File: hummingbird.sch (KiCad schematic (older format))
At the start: 43 parts, among them J1 JST, J2 ANEMOMETER, J3 USB_B_Micro, J4 Expansion, J5 SWD_PROG, J6 microSD, J7 SOIC_CLIP, J8 Conn_01x01_Female, J9 Conn_Coaxial, SW1 SW_DPDT_x2, U1 MCP73831-2-OT, U2 AP2112K-3.3, U3 W25Q64JVSSIM, U4 ATSAMD21G18A-AUT, U5 RFM95W-915S2, U6 BMP388, Y1 32.768 Hz

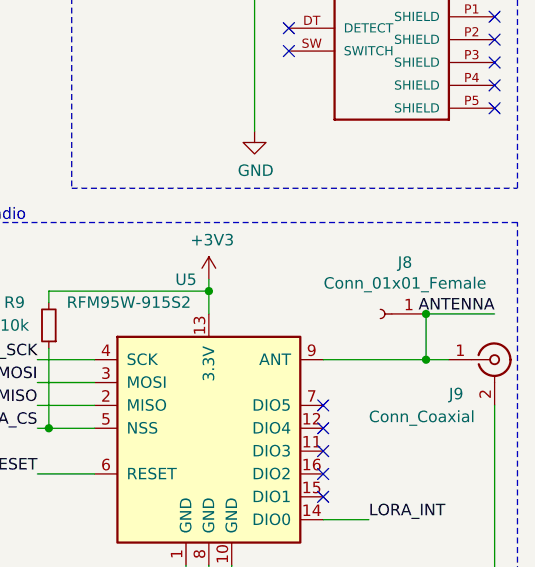
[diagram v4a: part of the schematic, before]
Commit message: add bmp388, SOICbyte and microSD footprint
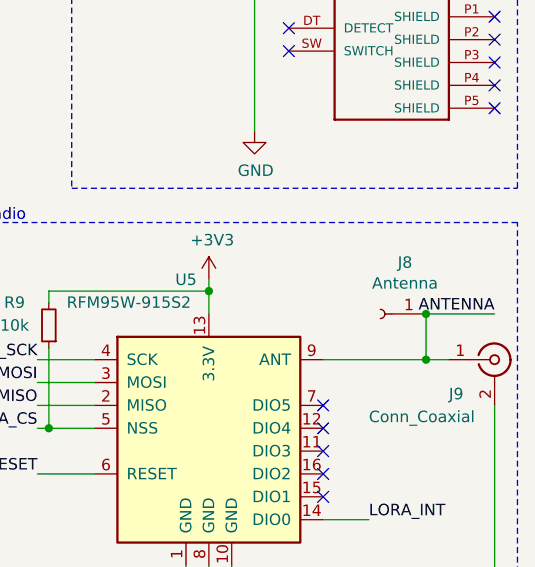
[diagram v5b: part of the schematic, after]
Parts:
- J6: footprint (none) -> microSD_503182-1852:MOLEX_503182-1852
- J7: footprint (none) -> footprints:SOIC_clipProgSmall
- J8: value Conn_01x01_Female -> Antenna; footprint (none) -> Connector_PinSocket_2.54mm:PinSocket_1x01_P2.54mm_Vertical
- U6: footprint (none) -> BMP388:PQFN50P200X200X80-10N
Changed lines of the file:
@@
 F 0 "U6" H 6800 6500 50  0000 C CNN
 F 1 "BMP388" H 6800 6400 50  0000 C CNN
-F 2 "" H 6800 5700 50  0001 L BNN
+F 2 "BMP388:PQFN50P200X200X80-10N" H 6800 5700 50  0001 L BNN
 F 3 "https://ae-bst.resource.bosch.com/media/_tech/media/datasheets/BST-BMP388-DS001.pdf" H 6800 5700 50  0001 L BNN
 F 4 "828-1079-1-ND" H 6800 5700 50  0001 L BNN "Field4"
@@
 F 0 "J6" H 9900 4467 50  0000 C CNN
 F 1 "microSD" H 9900 4376 50  0000 C CNN
-F 2 "" H 10400 3400 50  0001 L BNN
+F 2 "microSD_503182-1852:MOLEX_503182-1852" H 10400 3400 50  0001 L BNN
 F 3 "https://www.molex.com/pdm_docs/sd/5031821852_sd.pdf" H 10350 3750 50  0001 L BNN
 F 4 "MICRO SD NORMAL ULTRALOWPRO8CKTE" H 10350 4050 50  0001 L BNN "Field4"
@@
 P 9850 5150
 F 0 "J8" H 9742 4925 50  0000 C CNN
-F 1 "Conn_01x01_Female" H 9742 5016 50  0000 C CNN
-F 2 "" H 9850 5150 50  0001 C CNN
+F 1 "Antenna" H 9742 5016 50  0000 C CNN
+F 2 "Connector_PinSocket_2.54mm:PinSocket_1x01_P2.54mm_Vertical" H 9850 5150 50  0001 C CNN
 F 3 "~" H 9850 5150 50  0001 C CNN
 	1    9850 5150
@@
 F 0 "J7" H 4542 4375 50  0000 C CNN
 F 1 "SOIC_CLIP" H 4542 4466 50  0000 C CNN
-F 2 "" H 4650 4800 50  0001 C CNN
+F 2 "footprints:SOIC_clipProgSmall" H 4650 4800 50  0001 C CNN
 F 3 "https://hackaday.io/project/165917-soicbite-programmingdebug-connector-footprint" H 4650 4800 50  0001 C CNN
 	1    4650 4800

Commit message: copy all footprints to repo
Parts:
- C1, C10, C2, C3, C4, C5, C6, C7, C8, C9: footprint Capacitor_SMD:C_0603_1608Metric -> footprints:C_0603_1608Metric
- D1: footprint Diode_SMD:D_0603_1608Metric -> footprints:D_0603_1608Metric
- D2, D3, D4: footprint LED_SMD:LED_0603_1608Metric -> footprints:LED_0603_1608Metric
- J1: footprint (none) -> footprints:PinHeader_2x1mm_P2mm_SMD_RA
- J2: footprint Connector_PinHeader_2.54mm:PinHeader_1x03_P2.54mm_Vertical -> footprints:PinSocket_1x03_P2.54mm_Vertical
- J3: footprint (none) -> footprints:USB_Micro_B_Female_10118194-0001LF
- J4: footprint Connector_PinHeader_2.54mm:PinHeader_1x06_P2.54mm_Vertical -> footprints:PinSocket_1x06_P2.54mm_Vertical
- J5: footprint Connector_PinHeader_2.54mm:PinHeader_1x05_P2.54mm_Vertical -> footprints:PinSocket_1x05_P2.54mm_Vertical
- J8: footprint Connector_PinSocket_2.54mm:PinSocket_1x01_P2.54mm_Vertical -> footprints:PinSocket_1x01_P2.54mm_Vertical
- J9: footprint Connector_Coaxial:SMA_Molex_73251-1153_EdgeMount_Horizontal -> footprints:SMA_Molex_73251-1153_EdgeMount_Horizontal
- R1, R10, R2, R3, R4, R5, R6, R7, R8, R9: footprint Resistor_SMD:R_0603_1608Metric -> footprints:R_0603_1608Metric
- SW1: footprint (none) -> footprints:Switch_Slide_JS202011SCQN
- TP1, TP2: footprint TestPoint:TestPoint_Pad_D1.0mm -> footprints:TestPoint_Pad_D1.0mm
- U1, U2: footprint Package_TO_SOT_SMD:SOT-23-5 -> footprints:SOT-23-5
- U3: footprint Package_SO:SOIC-8_5.23x5.23mm_P1.27mm -> footprints:SOIC-8_5.23x5.23mm_P1.27mm
- U4: footprint Package_QFP:TQFP-48_7x7mm_P0.5mm -> footprints:TQFP-48_7x7mm_P0.5mm
- U5: footprint (none) -> footprints:RFM69HCW-XXXS2
- Y1: footprint Crystal:Crystal_SMD_3215-2Pin_3.2x1.5mm -> footprints:Crystal_SMD_3215-2Pin_3.2x1.5mm

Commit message: Add digikey part numbers
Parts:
- C1, C2, C3: DigiKey Part Number (none) -> 1276-1119-1-ND
- C10, C9: DigiKey Part Number (none) -> 1276-1182-1-ND
- C4, C5: DigiKey Part Number (none) -> 478-1167-1-ND
- C6, C7, C8: DigiKey Part Number (none) -> 311-1088-1-ND
- D1: DigiKey Part Number (none) -> 478-7798-1-ND
- D2, D3, D4: DigiKey Part Number (none) -> SML-D12U1WT86CT-ND
- J1: DigiKey Part Number (none) -> 455-1749-1-ND
- J3: symbol Connector:USB_B_Micro -> symbols:USB_B_Micro; DigiKey Part Number (none) -> 609-4618-1-ND
- J6: DigiKey Part Number (none) -> WM12834CT-ND
- J9: DigiKey Part Number (none) -> WM5534-ND
- R1, R3: DigiKey Part Number (none) -> RR08P100KDCT-ND
- R10, R4, R7, R8, R9: DigiKey Part Number (none) -> RHM10KADCT-ND
- R2, R5, R6: DigiKey Part Number (none) -> RHM1.0KDCT-ND
- SW1: DigiKey Part Number (none) -> 401-2002-1-ND
- U1: DigiKey Part Number (none) -> MCP73831T-2ACI/OTCT-ND
- U2: DigiKey Part Number (none) -> AP2112K-3.3TRG1DICT-ND
- U3: DigiKey Part Number (none) -> W25Q64JVSSIMCT-ND
- U4: DigiKey Part Number (none) -> ATSAMD21G18A-AUTCT-ND
- U5: DigiKey Part Number (none) -> RFM95W-915S2-ND
- U6: DigiKey Part Number (none) -> 828-1079-1-ND
- Y1: DigiKey Part Number (none) -> 535-9542-1-ND
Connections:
- net GND: now also J3.SH (Shield); no longer J3.6 (Shield)
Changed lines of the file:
@@
 F 2 "footprints:TQFP-48_7x7mm_P0.5mm" H 1500 3750 50  0001 C CNN
 F 3 "http://ww1.microchip.com/downloads/en/DeviceDoc/SAMD21-Family-DataSheet-DS40001882D.pdf" H 2450 6500 50  0001 C CNN
+F 4 "ATSAMD21G18A-AUTCT-ND" H 2450 5500 50  0001 C CNN "DigiKey Part Number"
 	1    2450 5500
 	1    0    0    -1
@@
 F 2 "footprints:C_0603_1608Metric" H 3500 3500 50  0001 C CNN
 F 3 "~" H 3500 3500 50  0001 C CNN
+F 4 "1276-1182-1-ND" H 3500 3500 50  0001 C CNN "DigiKey Part Number"
 	1    3500 3500
 	0    1    1    0
@@
 F 2 "footprints:C_0603_1608Metric" H 2650 3350 50  0001 C CNN
 F 3 "~" H 2650 3350 50  0001 C CNN
+F 4 "311-1088-1-ND" H 2650 3350 50  0001 C CNN "DigiKey Part Number"
 	1    2650 3350
 	0    1    1    0
@@
 F 2 "footprints:C_0603_1608Metric" H 2850 3200 50  0001 C CNN
 F 3 "~" H 2850 3200 50  0001 C CNN
+F 4 "311-1088-1-ND" H 2850 3200 50  0001 C CNN "DigiKey Part Number"
 	1    2850 3200
 	0    1    1    0
@@
 F 2 "footprints:C_0603_1608Metric" H 3050 3050 50  0001 C CNN
 F 3 "~" H 3050 3050 50  0001 C CNN
+F 4 "311-1088-1-ND" H 3050 3050 50  0001 C CNN "DigiKey Part Number"
 	1    3050 3050
 	0    1    1    0
@@
 F 2 "footprints:C_0603_1608Metric" H 2500 1800 50  0001 C CNN
 F 3 "~" H 2500 1800 50  0001 C CNN
+F 4 "1276-1119-1-ND" H 2500 1800 50  0001 C CNN "DigiKey Part Number"
 	1    2500 1800
 	1    0    0    -1
@@
 F 2 "footprints:D_0603_1608Metric" V 1000 1050 50  0001 C CNN
 F 3 "~" V 1000 1050 50  0001 C CNN
+F 4 "478-7798-1-ND" H 1000 1050 50  0001 C CNN "DigiKey Part Number"
 	1    1000 1050
 	0    -1   -1   0
@@
 F 2 "footprints:C_0603_1608Metric" H 750 1400 50  0001 C CNN
 F 3 "~" H 750 1400 50  0001 C CNN
+F 4 "1276-1119-1-ND" H 750 1400 50  0001 C CNN "DigiKey Part Number"
 	1    750  1400
 	1    0    0    -1
@@
 F 2 "footprints:SOT-23-5" H 6450 1100 50  0001 L CIN
 F 3 "http://ww1.microchip.com/downloads/en/DeviceDoc/20001984g.pdf" H 6250 1300 50  0001 C CNN
+F 4 "MCP73831T-2ACI/OTCT-ND" H 6400 1350 50  0001 C CNN "DigiKey Part Number"
 	1    6400 1350
 	1    0    0    -1
@@
 F 2 "footprints:LED_0603_1608Metric" H 7550 1450 50  0001 C CNN
 F 3 "~" H 7550 1450 50  0001 C CNN
+F 4 "SML-D12U1WT86CT-ND" H 7550 1450 50  0001 C CNN "DigiKey Part Number"
 	1    7550 1450
 	1    0    0    -1
@@
 F 2 "footprints:R_0603_1608Metric" H 7050 1450 50  0001 C CNN
 F 3 "~" H 7050 1450 50  0001 C CNN
+F 4 "RHM1.0KDCT-ND" H 7050 1450 50  0001 C CNN "DigiKey Part Number"
 	1    7050 1450
 	0    1    1    0
@@
 F 2 "footprints:C_0603_1608Metric" H 7300 1700 50  0001 C CNN
 F 3 "~" H 7300 1700 50  0001 C CNN
+F 4 "1276-1119-1-ND" H 7300 1700 50  0001 C CNN "DigiKey Part Number"
 	1    7300 1700
 	1    0    0    -1
@@
 F 2 "footprints:R_0603_1608Metric" H 5800 1450 50  0001 C CNN
 F 3 "~" H 5800 1450 50  0001 C CNN
+F 4 "RHM10KADCT-ND" H 5800 1450 50  0001 C CNN "DigiKey Part Number"
 	1    5800 1450
 	0    1    1    0
@@
 F 2 "footprints:PinHeader_2x1mm_P2mm_SMD_RA" H 8300 900 50  0001 C CNN
 F 3 "~" H 8300 900 50  0001 C CNN
+F 4 "455-1749-1-ND" H 8300 900 50  0001 C CNN "DigiKey Part Number"
 	1    8300 900
 	1    0    0    -1
@@
 $EndComp
 $Comp
-L Connector:USB_B_Micro J3
+L symbols:USB_B_Micro J3
 U 1 1 5CF892DE
 P 9450 1200
@@
 F 2 "footprints:USB_Micro_B_Female_10118194-0001LF" H 9600 1150 50  0001 C CNN
 F 3 "~" H 9600 1150 50  0001 C CNN
+F 4 "609-4618-1-ND" H 9450 1200 50  0001 C CNN "DigiKey Part Number"
 	1    9450 1200
 	1    0    0    -1
@@
 F 2 "footprints:Switch_Slide_JS202011SCQN" H 1350 1450 50  0001 C CNN
 F 3 "~" H 1350 1450 50  0001 C CNN
+F 4 "401-2002-1-ND" H 1350 1450 50  0001 C CNN "DigiKey Part Number"
 	1    1350 1450
 	0    1    1    0
@@
 F 2 "footprints:R_0603_1608Metric" H 8750 1050 50  0001 C CNN
 F 3 "~" H 8750 1050 50  0001 C CNN
+F 4 "RR08P100KDCT-ND" H 8750 1050 50  0001 C CNN "DigiKey Part Number"
 	1    8750 1050
 	-1   0    0    1
@@
 F 2 "footprints:R_0603_1608Metric" H 8750 1400 50  0001 C CNN
 F 3 "~" H 8750 1400 50  0001 C CNN
+F 4 "RR08P100KDCT-ND" H 8750 1400 50  0001 C CNN "DigiKey Part Number"
 	1    8750 1400
 	-1   0    0    1
@@
 F 7 "BMP388" H 6800 5700 50  0001 L BNN "Field7"
 F 8 "WFLGA-10 Bosch Tools" H 6800 5700 50  0001 L BNN "Field8"
+F 9 "828-1079-1-ND" H 6800 5700 50  0001 C CNN "DigiKey Part Number"
 	1    6800 5700
 	1    0    0    -1
@@
 F 7 "WM12834CT-ND" H 10300 3600 50  0001 L BNN "Field7"
 F 8 "https://www.digikey.com/product-detail/en/molex/5031821852/WM12834CT-ND/5823232?utm_source=snapeda&utm_medium=aggregator&utm_campaign=symbol" H 10350 3900 50  0001 L BNN "Field8"
+F 9 "WM12834CT-ND" H 9650 3600 50  0001 C CNN "DigiKey Part Number"
 	1    9650 3600
 	1    0    0    -1
@@
 F 2 "footprints:SOIC-8_5.23x5.23mm_P1.27mm" H 6750 3400 50  0001 C CNN
 F 3 "http://www.winbond.com/resource-files/w25q64jv%20revj%2003272018%20plus.pdf" H 6750 3400 50  0001 C CNN
+F 4 "W25Q64JVSSIMCT-ND" H 6750 3400 50  0001 C CNN "DigiKey Part Number"
 	1    6750 3400
 	1    0    0    -1
@@
 F 2 "footprints:RFM69HCW-XXXS2" H 5800 7300 50  0001 C CNN
 F 3 "https://www.hoperf.com/data/upload/portal/20181127/5bfcbea20e9ef.pdf" H 5800 7300 50  0001 C CNN
+F 4 "RFM95W-915S2-ND" H 9100 5650 50  0001 C CNN "DigiKey Part Number"
 	1    9100 5650
 	1    0    0    -1
@@
 F 2 "footprints:SMA_Molex_73251-1153_EdgeMount_Horizontal" H 10350 5350 50  0001 C CNN
 F 3 " ~" H 10350 5350 50  0001 C CNN
+F 4 "WM5534-ND" H 10350 5350 50  0001 C CNN "DigiKey Part Number"
 	1    10350 5350
 	1    0    0    -1
@@
 F 2 "footprints:LED_0603_1608Metric" H 3050 1200 50  0001 C CNN
 F 3 "~" H 3050 1200 50  0001 C CNN
+F 4 "SML-D12U1WT86CT-ND" H 3050 1200 50  0001 C CNN "DigiKey Part Number"
 	1    3050 1200
 	0    -1   -1   0
@@
 F 2 "footprints:LED_0603_1608Metric" H 3950 1050 50  0001 C CNN
 F 3 "~" H 3950 1050 50  0001 C CNN
+F 4 "SML-D12U1WT86CT-ND" H 3950 1050 50  0001 C CNN "DigiKey Part Number"
 	1    3950 1050
 	0    -1   -1   0
@@
 F 2 "footprints:R_0603_1608Metric" H 3050 1550 50  0001 C CNN
 F 3 "~" H 3050 1550 50  0001 C CNN
+F 4 "RHM1.0KDCT-ND" H 3050 1550 50  0001 C CNN "DigiKey Part Number"
 	1    3050 1550
 	1    0    0    -1
@@
 F 2 "footprints:R_0603_1608Metric" H 3950 1400 50  0001 C CNN
 F 3 "~" H 3950 1400 50  0001 C CNN
+F 4 "RHM1.0KDCT-ND" H 3950 1400 50  0001 C CNN "DigiKey Part Number"
 	1    3950 1400
 	1    0    0    -1
@@
 F 2 "footprints:Crystal_SMD_3215-2Pin_3.2x1.5mm" H 1150 3350 50  0001 C CNN
 F 3 "https://abracon.com/Resonators/ABS07.pdf" H 1150 3350 50  0001 C CNN
+F 4 "535-9542-1-ND" H 1150 3350 50  0001 C CNN "DigiKey Part Number"
 	1    1150 3350
 	1    0    0    -1
@@
 F 2 "footprints:C_0603_1608Metric" H 1000 2950 50  0001 C CNN
 F 3 "~" H 1000 2950 50  0001 C CNN
+F 4 "478-1167-1-ND" H 1000 2950 50  0001 C CNN "DigiKey Part Number"
 	1    1000 2950
 	-1   0    0    -1
@@
 F 2 "footprints:C_0603_1608Metric" H 1300 2950 50  0001 C CNN
 F 3 "~" H 1300 2950 50  0001 C CNN
+F 4 "478-1167-1-ND" H 1300 2950 50  0001 C CNN "DigiKey Part Number"
 	1    1300 2950
 	1    0    0    -1
@@
 F 2 "footprints:PinSocket_1x05_P2.54mm_Vertical" H 4650 3500 50  0001 C CNN
 F 3 "~" H 4650 3500 50  0001 C CNN
+F 4 "~" H 4650 3500 50  0001 C CNN "DigiKey Part Number"
 	1    4650 3500
 	-1   0    0    1
@@
 F 2 "footprints:C_0603_1608Metric" H 750 4000 50  0001 C CNN
 F 3 "~" H 750 4000 50  0001 C CNN
+F 4 "1276-1182-1-ND" H 750 4000 50  0001 C CNN "DigiKey Part Number"
 	1    750  4000
 	1    0    0    1
@@
 F 2 "footprints:PinSocket_1x03_P2.54mm_Vertical" H 4500 1100 50  0001 C CNN
 F 3 "~" H 4500 1100 50  0001 C CNN
+F 4 "~" H 4500 1100 50  0001 C CNN "DigiKey Part Number"
 	1    4500 1100
 	-1   0    0    1
@@
 F 2 "footprints:PinSocket_1x06_P2.54mm_Vertical" H 4500 2250 50  0001 C CNN
 F 3 "~" H 4500 2250 50  0001 C CNN
+F 4 "~" H 4500 2250 50  0001 C CNN "DigiKey Part Number"
 	1    4500 2250
 	-1   0    0    1
@@
 F 2 "footprints:SOT-23-5" H 1900 1975 50  0001 C CNN
 F 3 "https://www.diodes.com/assets/Datasheets/AP2112.pdf" H 1900 1750 50  0001 C CNN
+F 4 "AP2112K-3.3TRG1DICT-ND" H 1900 1650 50  0001 C CNN "DigiKey Part Number"
 	1    1900 1650
 	1    0    0    -1
@@
 F 2 "footprints:R_0603_1608Metric" H 6150 3050 50  0001 C CNN
 F 3 "~" H 6150 3050 50  0001 C CNN
+F 4 "RHM10KADCT-ND" H 6150 3050 50  0001 C CNN "DigiKey Part Number"
 	1    6150 3050
 	-1   0    0    1
@@
 F 2 "footprints:R_0603_1608Metric" H 9200 3000 50  0001 C CNN
 F 3 "~" H 9200 3000 50  0001 C CNN
+F 4 "RHM10KADCT-ND" H 9200 3000 50  0001 C CNN "DigiKey Part Number"
 	1    9200 3000
 	-1   0    0    1
@@
 F 2 "footprints:R_0603_1608Metric" H 8400 5200 50  0001 C CNN
 F 3 "~" H 8400 5200 50  0001 C CNN
+F 4 "RHM10KADCT-ND" H 8400 5200 50  0001 C CNN "DigiKey Part Number"
 	1    8400 5200
 	-1   0    0    1
@@
 F 2 "footprints:R_0603_1608Metric" H 6200 5300 50  0001 C CNN
 F 3 "~" H 6200 5300 50  0001 C CNN
+F 4 "RHM10KADCT-ND" H 6200 5300 50  0001 C CNN "DigiKey Part Number"
 	1    6200 5300
 	-1   0    0    1
@@
 F 2 "footprints:SOIC_clipProgSmall" H 4650 4800 50  0001 C CNN
 F 3 "https://hackaday.io/project/165917-soicbite-programmingdebug-connector-footprint" H 4650 4800 50  0001 C CNN
+F 4 "~" H 4650 4800 50  0000 C CNN "DigiKey Part Number"
 	1    4650 4800
 	-1   0    0    1

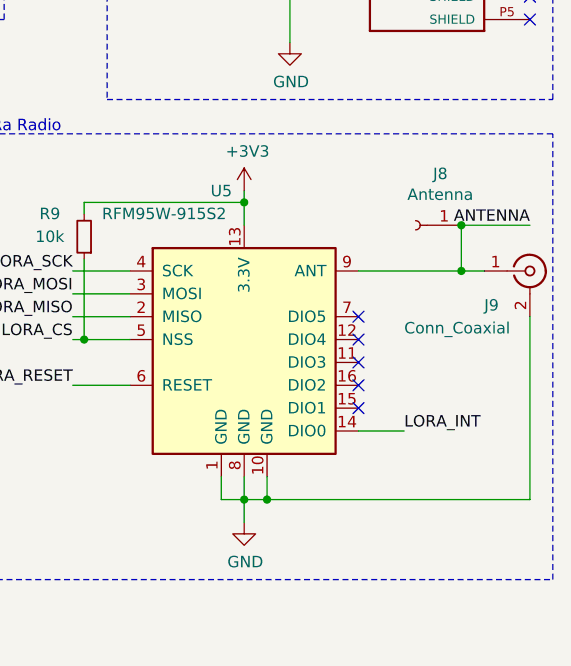
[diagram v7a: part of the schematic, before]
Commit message: remove SMA and some routing
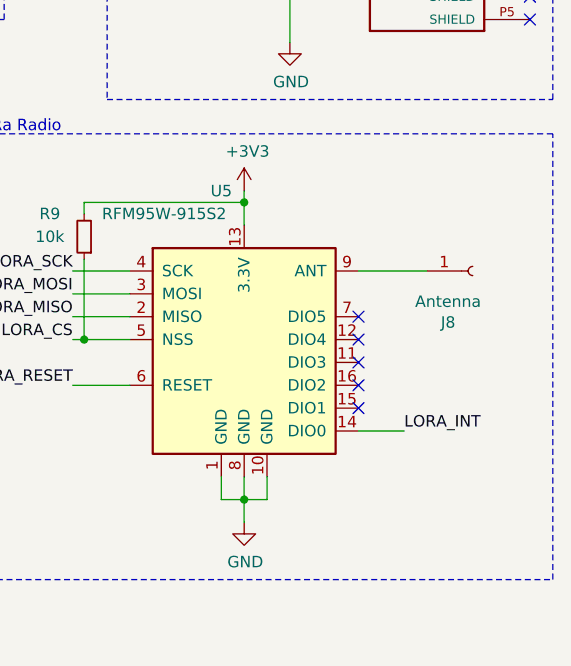
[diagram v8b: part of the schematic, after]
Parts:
- removed J9: Conn_Coaxial, footprints:SMA_Molex_73251-1153_EdgeMount_Horizontal, symbol Connector:Conn_Coaxial
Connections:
- net ANTENNA: no longer names the net of J8.1 (Pin_1), U5.9 (ANT)
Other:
- moved on the sheet: J8
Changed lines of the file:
@@
 Text Label 8350 5550 2    50   ~ 0
 LORA_MISO
-$Comp
-L Connector:Conn_Coaxial J9
-U 1 1 5D031A11
-P 10350 5350
-F 0 "J9" H 10150 5200 50  0000 L CNN
-F 1 "Conn_Coaxial" H 9800 5100 50  0000 L CNN
-F 2 "footprints:SMA_Molex_73251-1153_EdgeMount_Horizontal" H 10350 5350 50  0001 C CNN
-F 3 " ~" H 10350 5350 50  0001 C CNN
-F 4 "WM5534-ND" H 10350 5350 50  0001 C CNN "DigiKey Part Number"
-	1    10350 5350
-	1    0    0    -1
-$EndComp
-Wire Wire Line
-	9600 5350 10050 5350
-Wire Wire Line
-	10350 5550 10350 6350
-Wire Wire Line
-	10350 6350 9200 6350
 Wire Wire Line
 	9100 6350 9100 6250
 Wire Wire Line
 	9200 6250 9200 6350
-Connection ~ 9200 6350
 Wire Wire Line
 	9200 6350 9100 6350
@@
 	1    0    0    -1
 $EndComp
-Wire Wire Line
-	10050 5350 10050 5150
-Wire Wire Line
-	10050 5150 10350 5150
-Connection ~ 10050 5350
-Wire Wire Line
-	10050 5350 10150 5350
-Text Label 10350 5150 2    50   ~ 0
-ANTENNA
 Wire Wire Line
 	8600 5650 8400 5650
@@
 L Connector:Conn_01x01_Female J8
 U 1 1 5D2324C9
-P 9850 5150
-F 0 "J8" H 9742 4925 50  0000 C CNN
-F 1 "Antenna" H 9742 5016 50  0000 C CNN
-F 2 "footprints:PinSocket_1x01_P2.54mm_Vertical" H 9850 5150 50  0001 C CNN
-F 3 "~" H 9850 5150 50  0001 C CNN
-	1    9850 5150
-	-1   0    0    1
-$EndComp
-Connection ~ 10050 5150
+P 10100 5350
+F 0 "J8" H 9992 5125 50  0000 C CNN
+F 1 "Antenna" H 9992 5216 50  0000 C CNN
+F 2 "footprints:PinSocket_1x01_P2.54mm_Vertical" H 10100 5350 50  0001 C CNN
+F 3 "~" H 10100 5350 50  0001 C CNN
+	1    10100 5350
+	1    0    0    -1
+$EndComp
 $Comp
 L Regulator_Linear:AP2112K-3.3 U2
@@
 	9150 600  10300 600
 NoConn ~ 9450 3000
+Wire Wire Line
+	9600 5350 9900 5350
 $EndSCHEMATC
